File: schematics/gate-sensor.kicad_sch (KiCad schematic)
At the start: 16 parts, among them J1 Screw_Terminal_01x04, U1 LM2576T-5, U4 WeMos_D1_mini

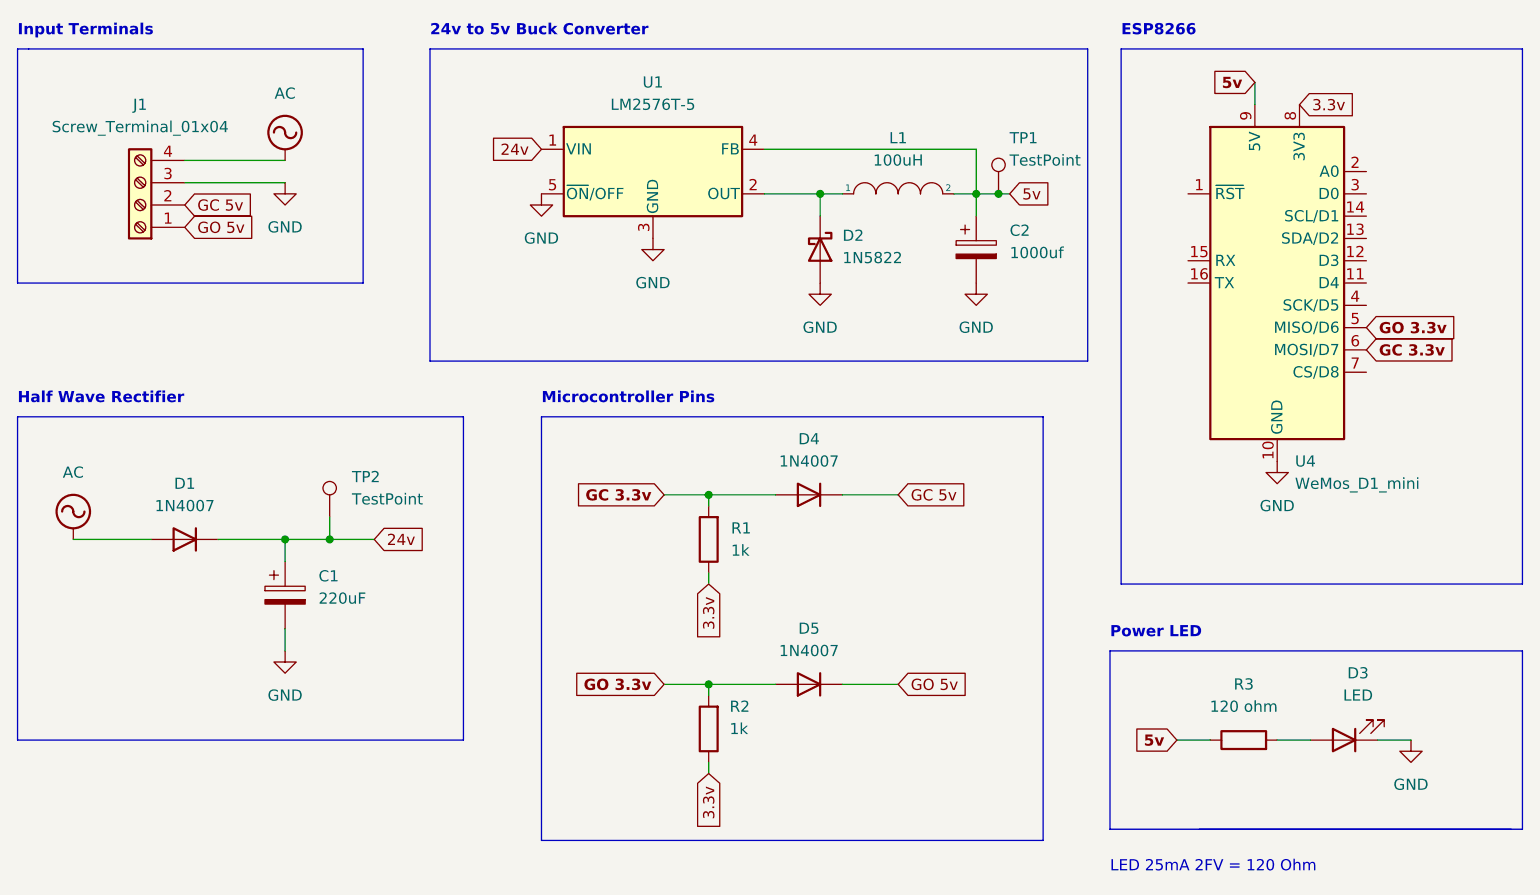
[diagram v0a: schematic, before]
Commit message: rename KiCad project
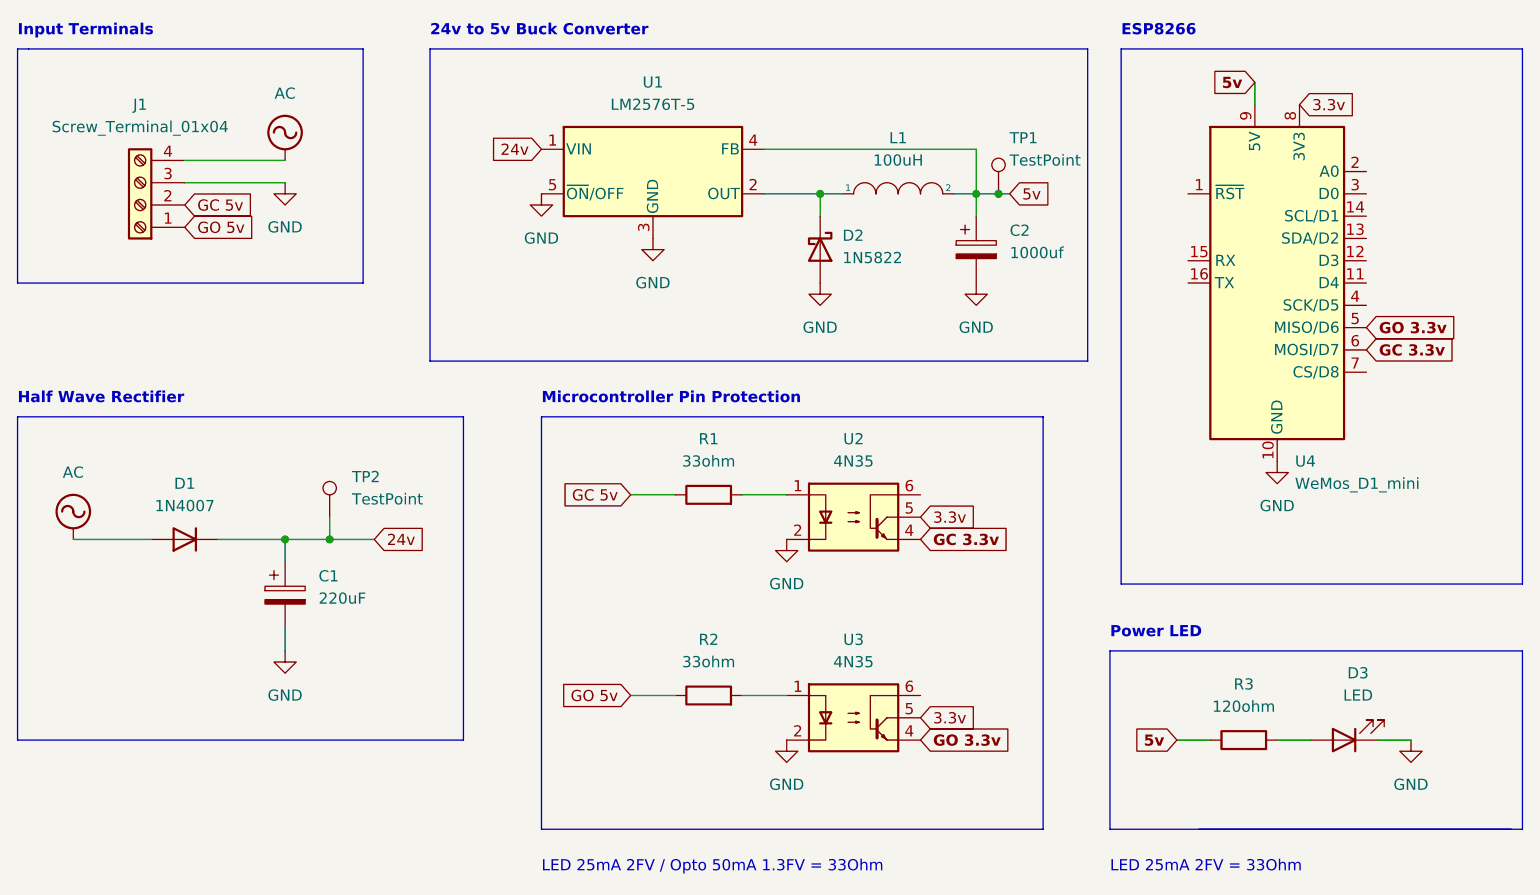
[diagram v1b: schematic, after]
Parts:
- removed D4, D5: 1N4007, Diode_THT:D_DO-41_SOD81_P10.16mm_Horizontal, symbol Diode:1N4007
- added U2, U3: 4N35, Package_DIP:DIP-6_W7.62mm, symbol Isolator:4N35
- R1, R2: value 1k -> 33ohm; footprint Resistor_SMD:R_0402_1005Metric -> Resistor_SMD:R_0603_1608Metric
- R3: value 120 ohm -> 120ohm
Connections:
- net 3.3v: now also U2.5, U3.5; no longer R1.1, R2.1
- net GC 3.3v: now also U2.4; no longer R1.2
- net GC 5v: now also R1.1
- net GND: now also U2.2, U3.2
- net GO 3.3v: now also U3.4; no longer R2.2
- net GO 5v: now also R2.1
- new net: R1.2, U2.1
- new net: R2.2, U3.1
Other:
- note added: "LED 25mA 2FV / Opto 50mA 1.3FV = 33Ohm"
- note added: "LED 25mA 2FV = 33Ohm"
- note added: "Microcontroller Pin Protection"
- note removed: "LED 25mA 2FV = 120 Ohm"
- note removed: "Microcontroller Pins"
